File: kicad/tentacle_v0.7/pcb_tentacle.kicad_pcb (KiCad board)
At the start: 2 copper layers, 100 x 165 mm, 961 parts, among them J1302 Conn_02x20, J1303 Conn_02x20, J1501 Conn_02x20, J1502 Conn_01x12, J201 Conn_02x05, J202 Conn_01x5, J301 USB_C_Receptacle_USB2.0, J501 Conn_02x20, U1001 GAQY221S, U1101 GAQY221S, U1201 GAQY221S, U1501 RP2040, U1502 W25Q32JVS, U1503 TXB0108PW, U1504 TXB0108PW, U201 RP2040, U202 AMS1117-3.3, U203 W25Q32JVS, U204 TPS2595xx, U205 TPS2595xx, U207 TPS2595xx, U302 USB2514B_Bi, U601 GAQY221S, U701 GAQY221S, U801 GAQY221S, U901 GAQY221S, X201 Oscillator-12MHz, Y301 24MHz

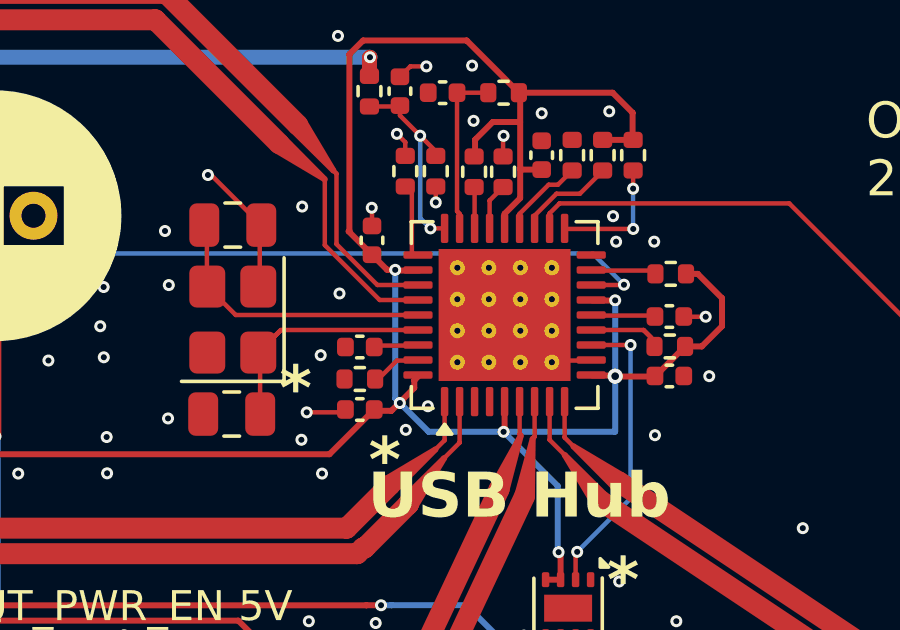
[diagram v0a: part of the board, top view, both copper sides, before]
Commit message: USB hub footprint: hole 0.2 mm -> 0.3 mm
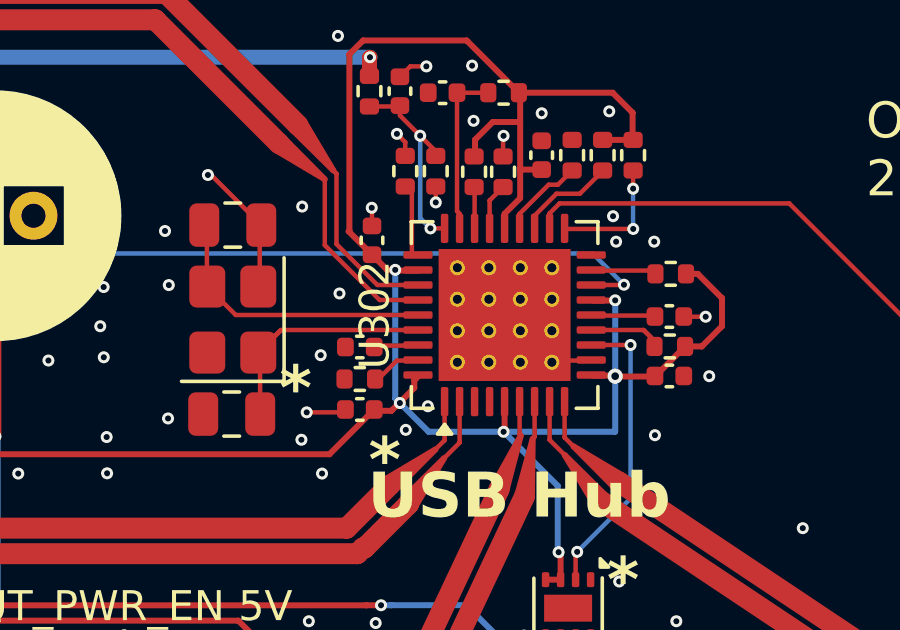
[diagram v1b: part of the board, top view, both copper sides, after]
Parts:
- U302: footprint Package_DFN_QFN:Texas_RHH0036C_VQFN-36-1EP_6x6mm_P0.5mm_EP4.4x4.4mm_ThermalVias -> 00_project_library:Texas_RHH0036C_VQFN-36-1EP_6x6mm_P0.5mm_EP4.4x4.4mm_ThermalVias
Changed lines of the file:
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@@
 		(embedded_fonts no)
 	)
-	(footprint "Package_DFN_QFN:Texas_RHH0036C_VQFN-36-1EP_6x6mm_P0.5mm_EP4.4x4.4mm_ThermalVias"
+	(footprint "00_project_library:Texas_RHH0036C_VQFN-36-1EP_6x6mm_P0.5mm_EP4.4x4.4mm_ThermalVias"
 		(layer "F.Cu")
 		(at 117.365 28.6324 90)
@@
 			(at 0 -4.33 90)
 			(layer "F.SilkS")
-			(hide yes)
 			(effects
 				(font
@@
 			(at -1.575 -1.575 90)
 			(size 0.5 0.5)
-			(drill 0.2)
+			(drill 0.3)
 			(property pad_prop_heatsink)
 			(layers "*.Cu")
@@
 			(at -1.575 -0.525 90)
 			(size 0.5 0.5)
-			(drill 0.2)
+			(drill 0.3)
 			(property pad_prop_heatsink)
 			(layers "*.Cu")
@@
 			(at -1.575 0.525 90)
 			(size 0.5 0.5)
-			(drill 0.2)
+			(drill 0.3)
 			(property pad_prop_heatsink)
 			(layers "*.Cu")
@@
 			(at -1.575 1.575 90)
 			(size 0.5 0.5)
-			(drill 0.2)
+			(drill 0.3)
 			(property pad_prop_heatsink)
 			(layers "*.Cu")
@@
 			(at -0.525 -1.575 90)
 			(size 0.5 0.5)
-			(drill 0.2)
+			(drill 0.3)
 			(property pad_prop_heatsink)
 			(layers "*.Cu")
@@
 			(at -0.525 -0.525 90)
 			(size 0.5 0.5)
-			(drill 0.2)
+			(drill 0.3)
 			(property pad_prop_heatsink)
 			(layers "*.Cu")
@@
 			(at -0.525 0.525 90)
 			(size 0.5 0.5)
-			(drill 0.2)
+			(drill 0.3)
 			(property pad_prop_heatsink)
 			(layers "*.Cu")
@@
 			(at -0.525 1.575 90)
 			(size 0.5 0.5)
-			(drill 0.2)
+			(drill 0.3)
 			(property pad_prop_heatsink)
 			(layers "*.Cu")
@@
 			(at 0.525 -1.575 90)
 			(size 0.5 0.5)
-			(drill 0.2)
+			(drill 0.3)
 			(property pad_prop_heatsink)
 			(layers "*.Cu")
@@
 			(at 0.525 -0.525 90)
 			(size 0.5 0.5)
-			(drill 0.2)
+			(drill 0.3)
 			(property pad_prop_heatsink)
 			(layers "*.Cu")
@@
 			(at 0.525 0.525 90)
 			(size 0.5 0.5)
-			(drill 0.2)
+			(drill 0.3)
 			(property pad_prop_heatsink)
 			(layers "*.Cu")
@@
 			(at 0.525 1.575 90)
 			(size 0.5 0.5)
-			(drill 0.2)
+			(drill 0.3)
 			(property pad_prop_heatsink)
 			(layers "*.Cu")
@@
 			(at 1.575 -1.575 90)
 			(size 0.5 0.5)
-			(drill 0.2)
+			(drill 0.3)
 			(property pad_prop_heatsink)
 			(layers "*.Cu")
@@
 			(at 1.575 -0.525 90)
 			(size 0.5 0.5)
-			(drill 0.2)
+			(drill 0.3)
 			(property pad_prop_heatsink)
 			(layers "*.Cu")
@@
 			(at 1.575 0.525 90)
 			(size 0.5 0.5)
-			(drill 0.2)
+			(drill 0.3)
 			(property pad_prop_heatsink)
 			(layers "*.Cu")
@@
 			(at 1.575 1.575 90)
 			(size 0.5 0.5)
-			(drill 0.2)
-			(property pad_prop_heatsink)
-			(layers "*.Cu")
+			(drill 0.3)
+			(property pad_prop_heatsink)
+			(layers "*.Cu")
